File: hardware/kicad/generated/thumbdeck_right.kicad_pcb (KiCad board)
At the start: 2 copper layers, 74.5 x 109.5 mm, 74 parts, among them SW1 SNAP7, SW10 SNAP7, SW11 SNAP7, SW12 SNAP7, SW13 SNAP7, SW14 SNAP7, SW15 SNAP7, SW16 SNAP7, SW17 SNAP7, SW18 SNAP7, SW19 SNAP7, SW2 SNAP7, SW20 SNAP7, SW21 SNAP7, SW22 SNAP7, SW23 SNAP7, SW24 SNAP7, SW25 SNAP7, SW26 SNAP7, SW27 SNAP7, SW28 SNAP7, SW29 SNAP7, SW3 SNAP7, SW30 SNAP7, SW31 SNAP7, SW32 SNAP7, SW33 SNAP7, SW34 SNAP7, SW35 SNAP7, SW36 SNAP7, SW37 SNAP7, SW4 SNAP7, SW5 SNAP7, SW6 SNAP7, SW7 SNAP7, SW8 SNAP7, SW9 SNAP7

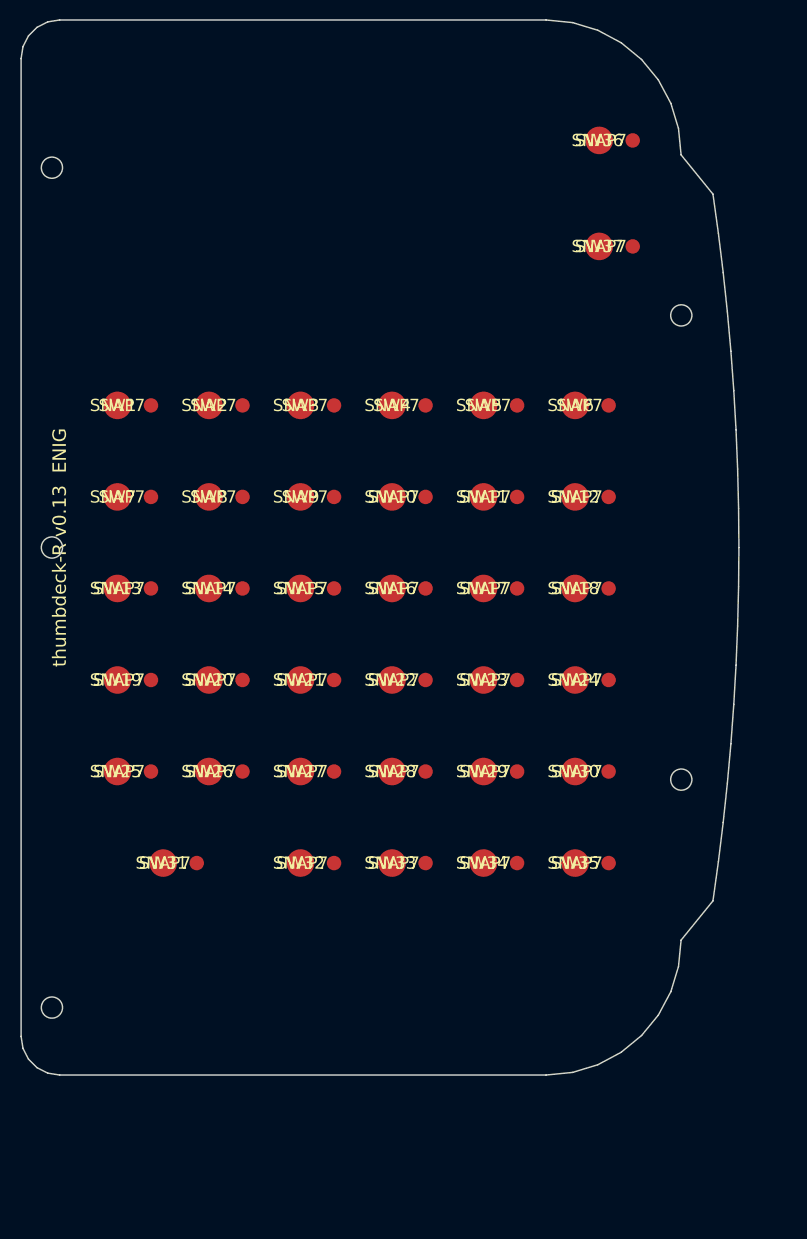
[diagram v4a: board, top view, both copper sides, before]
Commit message: Autonomous route+validate loop working (KiCad 9 + Freerouting)
- Upgraded toolchain: KiCad 9 (drc/render CLI + Specctra API), Freerouting 2.2.4
  (Java 25). gen_board.py places real footprints (Snaptron dome, marbastlib E73,
  stock USB-C/SOT-23/SOD-323/0402) + full netlist; route.sh runs the loop:
  DSN export -> Freerouting autoroute -> SES import -> DRC(json) -> 2D+3D render.
- Solved the headless blockers: Specctra export chokes on the custom dome pad and
  the MountingHole footprint -> use simple circular dome pads + Edge.Cuts holes.
- First autoroute of the right grip: 780 tracks + 100 vias; DRC 34 violations /
  44 unconnected (iterating to clean). E73 pin-map + wiring in docs/routing-status.md.

Co-Authored-By: Claude Opus 4.8 <noreply@anthropic.com>
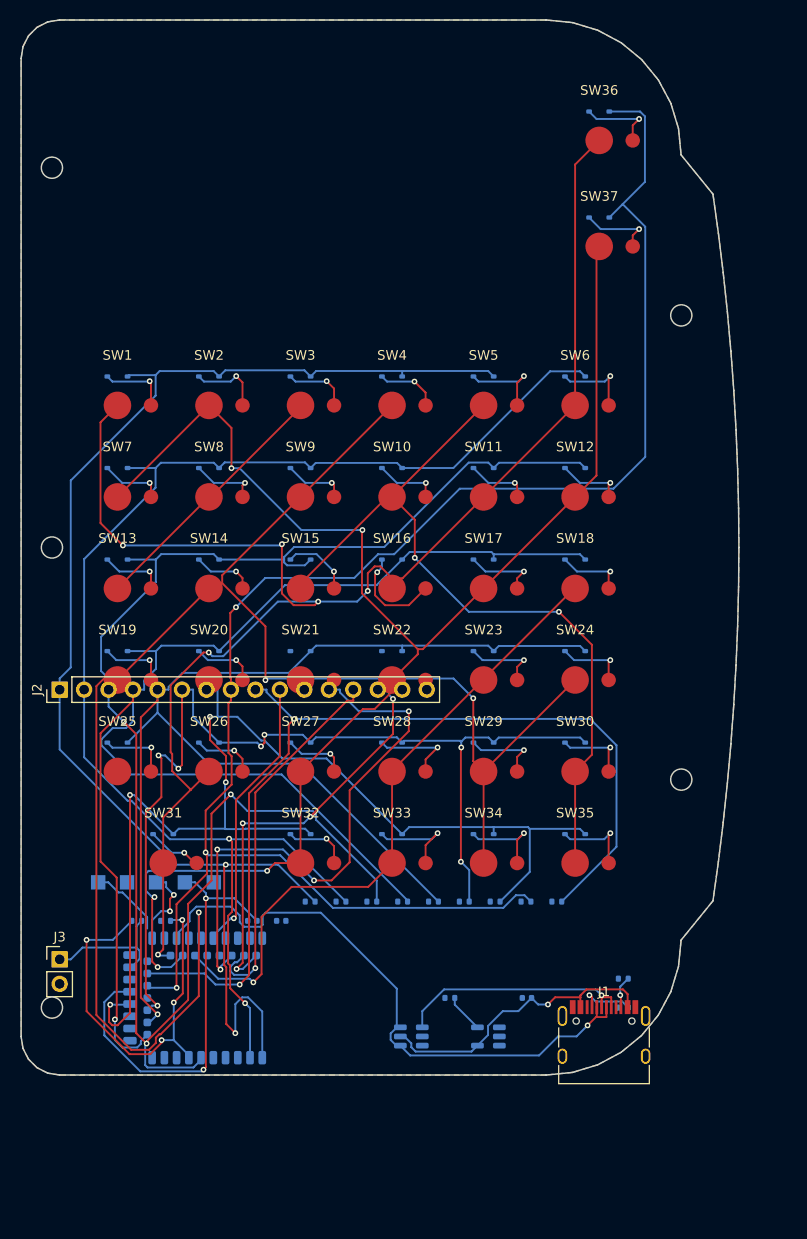
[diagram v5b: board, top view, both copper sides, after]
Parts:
- added C1: 1uF, C_0402_1005Metric, B.Cu at (24.0, 93.5)
- added C2: 100nF, C_0402_1005Metric, B.Cu at (27.0, 93.5)
- added C3: 4u7, C_0402_1005Metric, B.Cu at (52.5, 101.5)
- added J1: USB-C, USB_C_Receptacle_HRO_TYPE-C-31-M-12, F.Cu at (60.5, 106.5)
- added J2: BRIDGE_16, PinHeader_1x16_P2.54mm_Vertical, F.Cu at (4.00, 69.5)
- added J3: LiPo, PinHeader_1x02_P2.54mm_Vertical, F.Cu at (4.00, 97.5)
- added R1: 4k7, R_0402_1005Metric, B.Cu at (30.0, 91.5)
- added R2: 4k7, R_0402_1005Metric, B.Cu at (33.2, 91.5)
- added R20: 5k1, R_0402_1005Metric, B.Cu at (62.5, 102.5)
- added R21: 5k1, R_0402_1005Metric, B.Cu at (62.5, 99.5)
- added R22: 1M, R_0402_1005Metric, B.Cu at (12.0, 93.5)
- added R23: 1M, R_0402_1005Metric, B.Cu at (15.0, 93.5)
- added R24: 2k, R_0402_1005Metric, B.Cu at (44.5, 101.5)
- added R3: 4k7, R_0402_1005Metric, B.Cu at (36.4, 91.5)
- added R4: 4k7, R_0402_1005Metric, B.Cu at (39.6, 91.5)
- added R5: 4k7, R_0402_1005Metric, B.Cu at (42.8, 91.5)
- added R6: 4k7, R_0402_1005Metric, B.Cu at (46.0, 91.5)
- added R7: 4k7, R_0402_1005Metric, B.Cu at (49.2, 91.5)
- added R8: 4k7, R_0402_1005Metric, B.Cu at (52.4, 91.5)
- added R9: 4k7, R_0402_1005Metric, B.Cu at (55.6, 91.5)
- added TP1: SWDIO, TestPoint_Pad_1.5x1.5mm, B.Cu at (8.00, 89.5)
- added TP2: SWDCLK, TestPoint_Pad_1.5x1.5mm, B.Cu at (11.0, 89.5)
- added TP3: RESET, TestPoint_Pad_1.5x1.5mm, B.Cu at (14.0, 89.5)
- added TP4: 3V3, TestPoint_Pad_1.5x1.5mm, B.Cu at (17.0, 89.5)
- added TP5: GND, TestPoint_Pad_1.5x1.5mm, B.Cu at (20.0, 89.5)
- added U1: E73-2G4M08S1C, nRF52840_E73-2G4M08S1C, B.Cu at (20.0, 101.5)
- added U2: MCP73831, SOT-23-5, B.Cu at (48.5, 105.5)
- added U3: USBLC6-2SC6, SOT-23-6, B.Cu at (40.5, 105.5)
- SW1, SW10, SW11, SW12, SW13, SW14, SW15, SW16, SW17, SW18, SW19, SW2, SW20, SW21, SW22, SW23, SW24, SW25, SW26, SW27, SW28, SW29, SW3, SW30, SW31, SW32, SW33, SW34, SW35, SW36, SW37, SW4, SW5, SW6, SW7, SW8, SW9: footprint (none) -> snaptron_7mm_simple
- moved D36 2.80 mm to (60.0, 9.50), turned to 180 degrees
- moved D37 2.80 mm to (60.0, 20.5), turned to 180 degrees
- moved D1 2.80 mm to (10.0, 37.0), turned to 180 degrees
- moved D10 2.80 mm to (38.5, 46.5), turned to 180 degrees
- moved D11 2.80 mm to (48.0, 46.5), turned to 180 degrees
- moved D12 2.80 mm to (57.5, 46.5), turned to 180 degrees
- moved D13 2.80 mm to (10.0, 56.0), turned to 180 degrees
- moved D14 2.80 mm to (19.5, 56.0), turned to 180 degrees
- moved D15 2.80 mm to (29.0, 56.0), turned to 180 degrees
- moved D16 2.80 mm to (38.5, 56.0), turned to 180 degrees
- moved D17 2.80 mm to (48.0, 56.0), turned to 180 degrees
- moved D18 2.80 mm to (57.5, 56.0), turned to 180 degrees
- moved D19 2.80 mm to (10.0, 65.5), turned to 180 degrees
- moved D2 2.80 mm to (19.5, 37.0), turned to 180 degrees
- moved D20 2.80 mm to (19.5, 65.5), turned to 180 degrees
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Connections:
- net D_R1 renamed DN_R1
- net D_R10 renamed DN_R10
- net D_R11 renamed DN_R11
- net D_R12 renamed DN_R12
- net D_R13 renamed DN_R13
- net D_R14 renamed DN_R14
- net D_R15 renamed DN_R15
- net D_R16 renamed DN_R16
- net D_R17 renamed DN_R17
- net D_R18 renamed DN_R18
- net D_R19 renamed DN_R19
- net D_R2 renamed DN_R2
- net D_R20 renamed DN_R20
- net D_R21 renamed DN_R21
- net D_R22 renamed DN_R22
- net D_R23 renamed DN_R23
- net D_R24 renamed DN_R24
- net D_R25 renamed DN_R25
- net D_R26 renamed DN_R26
- net D_R27 renamed DN_R27
- net D_R28 renamed DN_R28
- net D_R29 renamed DN_R29
- net D_R3 renamed DN_R3
- net D_R30 renamed DN_R30
- net D_R31 renamed DN_R31
- net D_R32 renamed DN_R32
- net D_R33 renamed DN_R33
- net D_R34 renamed DN_R34
- net D_R35 renamed DN_R35
- net D_R36 renamed DN_R36
- net D_R37 renamed DN_R37
- net D_R4 renamed DN_R4
- net D_R5 renamed DN_R5
- net D_R6 renamed DN_R6
- net D_R7 renamed DN_R7
- net D_R8 renamed DN_R8
- net D_R9 renamed DN_R9
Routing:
- net ROW7: track 0.00 -> 174.7 mm, vias 0 -> 3
- net ROW2: track 0.00 -> 170.6 mm, vias 0 -> 3
- net COL3: track 0.00 -> 170.3 mm, vias 0 -> 3
- net COL0: track 0.00 -> 162.6 mm, vias 0 -> 6
- net COL1: track 0.00 -> 160.0 mm, vias 0 -> 5
- net ROW3: track 0.00 -> 148.2 mm, vias 0 -> 1
- net ROW0: track 0.00 -> 145.6 mm, vias 0 -> 2
- net ROW1: track 0.00 -> 143.7 mm, vias 0 -> 2
- net ROW4: track 0.00 -> 128.3 mm, vias 0 -> 1
- net ROW6: track 0.00 -> 120.8 mm, vias 0 -> 4
- net ROW5: track 0.00 -> 105.1 mm, vias 0 -> 7
- net ROW8: track 0.00 -> 98.6 mm, vias 0 -> 2
- net COL2: track 0.00 -> 93.7 mm, vias 0 -> 1
- net COL4: track 0.00 -> 79.9 mm, vias 0 -> 2
- net USB_DM: track 0.00 -> 63.4 mm, vias 0 -> 1
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- added copper zone on B.Cu, net GND
- added copper zone on F.Cu, net GND
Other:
- board text removed: "ANTENNA"
- board text removed: "BRIDGE"
- board text removed: "CHARGER"
- board text removed: "CONTROLLER"
- board text removed: "ROUTING + MODULE/CONN FOOTPRINTS = NEXT GATE"
- board text removed: "TRACKPAD-TPS43-OPT"
- board text removed: "USB_C"
- board text removed: "thumbdeck-R v0.13 ENIG"

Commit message: v0.14: verified-correct 4-layer board, real firmware, 3D shells/keymats + fit-check
PCB / electrical (audited vs datasheets + adversarial multi-lens review):
- FIX blocker: USBLC6-2SC6 ESD shorted USB D+ to D- (pin6 == pin1 node). Rewire
  D+=pins1&6, D-=pins3&4 per ST datasheet.
- Verified E73 pinmap 1:1 vs the official Ebyte datasheet (the "silent killer" is clean).
- Charger R24 2k->5k1 (~505mA -> ~196mA, ~0.5C of a 400mAh cell).
- Fix left-grip bridge header on wrong edge; rotate left-grip switch pads (ring-pad
  direction) so they clear the inner connector.
- Single-sided back assembly: move all reflow parts to B.Cu; connectors J2/J3 to back
  so they clear the top shell + keymat.
- Move bridge cols COL6-9 off the module inner pads to castellated edge pads; cluster
  USB-C/ESD/charger by the module (short D+/D-); add VBAT bulk cap.
- Convert to 4-layer (F/GND-plane/signal/B): RF ground reference + routable fan-in.
- Both grips pass placement DRC clean (0 non-silk violations).

Simulation: sim_matrix.py proves the 79-key col2row matrix is ghosting-free across
~68.5k finger-press scenarios (0 failures; no-diode control ghosts ~35k -> sim is real).

Firmware: replace the stale 50-key nice!nano shield with a generated E73 (nRF52840)
board -- 9x10, 79 keys, real nRF pins + transform/keymap derived from the PCB model
(gen_firmware.py) so hardware and firmware can't drift.

3D CAD (docs/cad-process.md): deck3d.py builds, from the SAME deck.py model, the PCB
fit-model (real component dims), one-piece back shell, front shell (79 key openings +
phone window), keymats, and the LiPo/flex/phone/MagSafe -- assembled + collision-checked
to 0 impossible overlaps (the loop caught+fixed a battery-through-floor + front-connector
clashes). STL/STEP in hardware/cad/models/; renders added.

Docs: authoritative docs/evaluation.md; superseded banners on drifted docs; README gets
3D renders + updated reproduce/routing notes. Trackpad deferred for v1.

Remaining gates: finish the 4-laye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
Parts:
- added C4: 4u7, C_0805_2012Metric, B.Cu at (6.00, 96.5)
- J1, J3: moved to B.Cu
- J2: footprint PinHeader_1x16_P2.54mm_Vertical -> PinHeader_2x08_P2.54mm_Vertical; moved to B.Cu
- R24: value 2k -> 5k1
- moved J3 54.4 mm to (58.0, 104.0), turned to 180 degrees
- moved R20 27.7 mm to (35.0, 99.5)
- moved R21 24.5 mm to (38.0, 99.5)
- moved J1 23.5 mm to (37.0, 105.5), turned to 180 degrees
- moved C2 19.3 mm to (9.00, 100.5)
- moved C1 18.0 mm to (9.00, 103.5)
- moved R22 11.7 mm to (6.00, 103.5)
- moved R23 11.4 mm to (6.00, 100.5)
- moved R24 8.50 mm to (53.0, 101.5)
- moved U3 6.52 mm to (47.0, 106.0)
- moved TP1 6.32 mm to (14.0, 91.5)
- moved TP2 6.32 mm to (17.0, 91.5)
- moved TP3 6.32 mm to (20.0, 91.5)
- moved TP4 6.32 mm to (23.0, 91.5)
- moved TP5 6.32 mm to (26.0, 91.5)
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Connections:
- U1 pad 10: (no net) -> COL8
- U1 pad 11: (no net) -> COL9
- U1 pad 15: SDA -> (no net)
- U1 pad 3: (no net) -> COL6
- U1 pad 36: COL6 -> (no net)
- U1 pad 38: COL7 -> (no net)
- U1 pad 4: SCL -> (no net)
- U1 pad 40: COL8 -> (no net)
- U1 pad 42: COL9 -> (no net)
- U1 pad 8: TP_DR -> (no net)
- U1 pad 9: (no net) -> COL7
- U3 pad 3: (no net) -> USB_DM
- U3 pad 6: USB_DM -> USB_DP
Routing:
- net ROW7: track 174.7 -> 0.00 mm, vias 3 -> 0
- net ROW2: track 170.6 -> 0.00 mm, vias 3 -> 0
- net COL3: track 170.3 -> 0.00 mm, vias 3 -> 0
- net COL0: track 162.6 -> 0.00 mm, vias 6 -> 0
- net COL1: track 160.0 -> 0.00 mm, vias 5 -> 0
- net ROW3: track 148.2 -> 0.00 mm, vias 1 -> 0
- net ROW0: track 145.6 -> 0.00 mm, vias 2 -> 0
- net ROW1: track 143.7 -> 0.00 mm, vias 2 -> 0
- net ROW4: track 128.3 -> 0.00 mm, vias 1 -> 0
- net ROW6: track 120.8 -> 0.00 mm, vias 4 -> 0
- net ROW5: track 105.1 -> 0.00 mm, vias 7 -> 0
- net ROW8: track 98.6 -> 0.00 mm, vias 2 -> 0
- net COL2: track 93.7 -> 0.00 mm, vias 1 -> 0
- net COL4: track 79.9 -> 0.00 mm, vias 2 -> 0
- net USB_DM: track 63.4 -> 0.00 mm, vias 1 -> 0
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- added copper zone on In1.Cu, net GND
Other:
- copper layers 2 -> 4
